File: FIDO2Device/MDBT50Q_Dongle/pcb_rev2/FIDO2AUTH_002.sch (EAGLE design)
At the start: 33 parts, among them CN1 TE-1734028, CN2 IF_5PIN_H, CN3 IF_3PIN, SW1 SKRPACE010, SW2 SKTADAE010, U1 MDBT50Q-P1M, U2 XC6206P332MR-G, X1 NX3215SA-32.768K

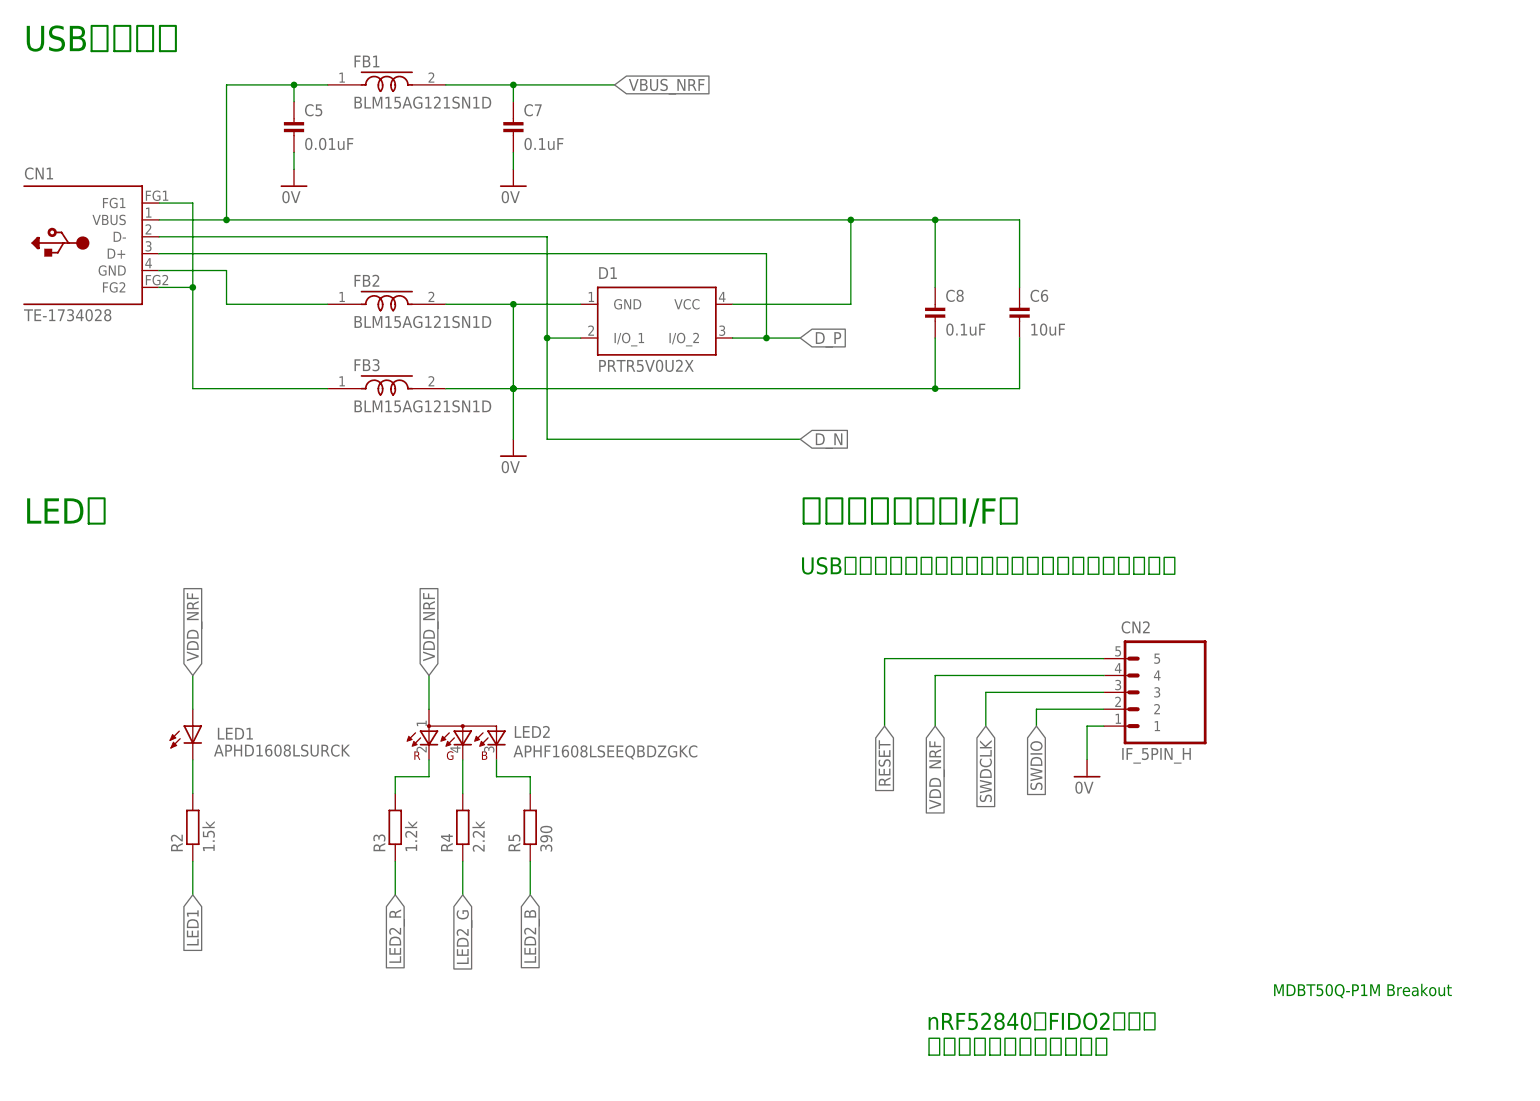
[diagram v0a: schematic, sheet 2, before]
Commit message: 回路図・部品表を修正
・増えた部品は２点（LED3、R6）
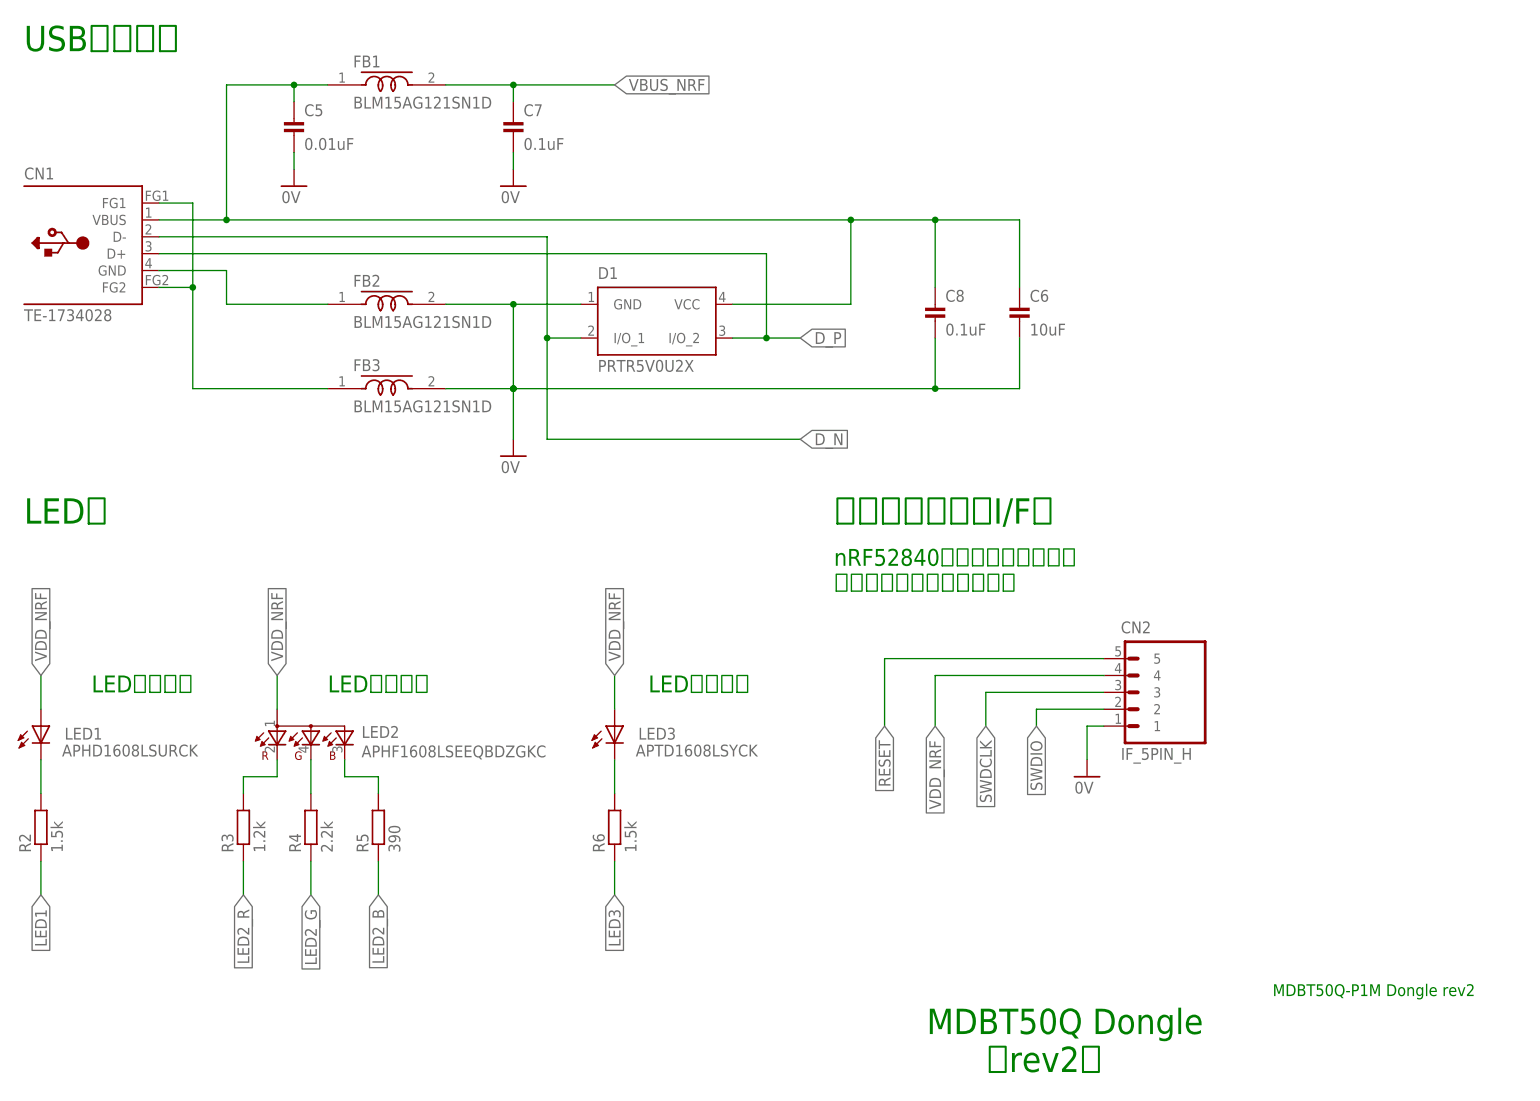
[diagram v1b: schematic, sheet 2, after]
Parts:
- added LED3: APTD1608LSYCK, Parts:APTD1608LSYCK
- added R6: 1.5k, Parts:RESISTOR_0603
- U1: device Parts:MDBT50Q-P1M -> Modules:MDBT50Q-P1M
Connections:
- removed net AIN1: CN3.3, U1.P0.03/AIN1
- new net LED3: R6.1, U1.P0.26
- new net N$8: LED3.C, R6.2
- new net UART_TX: CN3.2, U1.P0.06
- net AIN0: now also CN3.3; no longer CN3.2
- net LED1: now also U1.P1.10; no longer U1.P0.06
- net VDD_NRF: now also LED3.A
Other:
- note added: "LED（赤色）"
- note added: "LED（黄色）"
- note added: "LED（３色）"
- note added: "MDBT50Q Dongle （rev2）"
- note added: "MDBT50Q-P1M Dongle rev2"
- note added: "nRF52840アプリケーションを 書込する際に使用します。"
- note removed: "MDBT50Q-P1M Breakout"
- note removed: "USBブートローダーを初期書込する際に使用します。"
- note removed: "nRF52840版FIDO2認証器 開発用ブレークアウト基板"
- moved on the sheet: LED1, LED2, R2, R3, R4, R5
